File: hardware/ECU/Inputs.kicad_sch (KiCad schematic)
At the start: 39 parts, among them U12 LMV324LIDT, U13 SP720

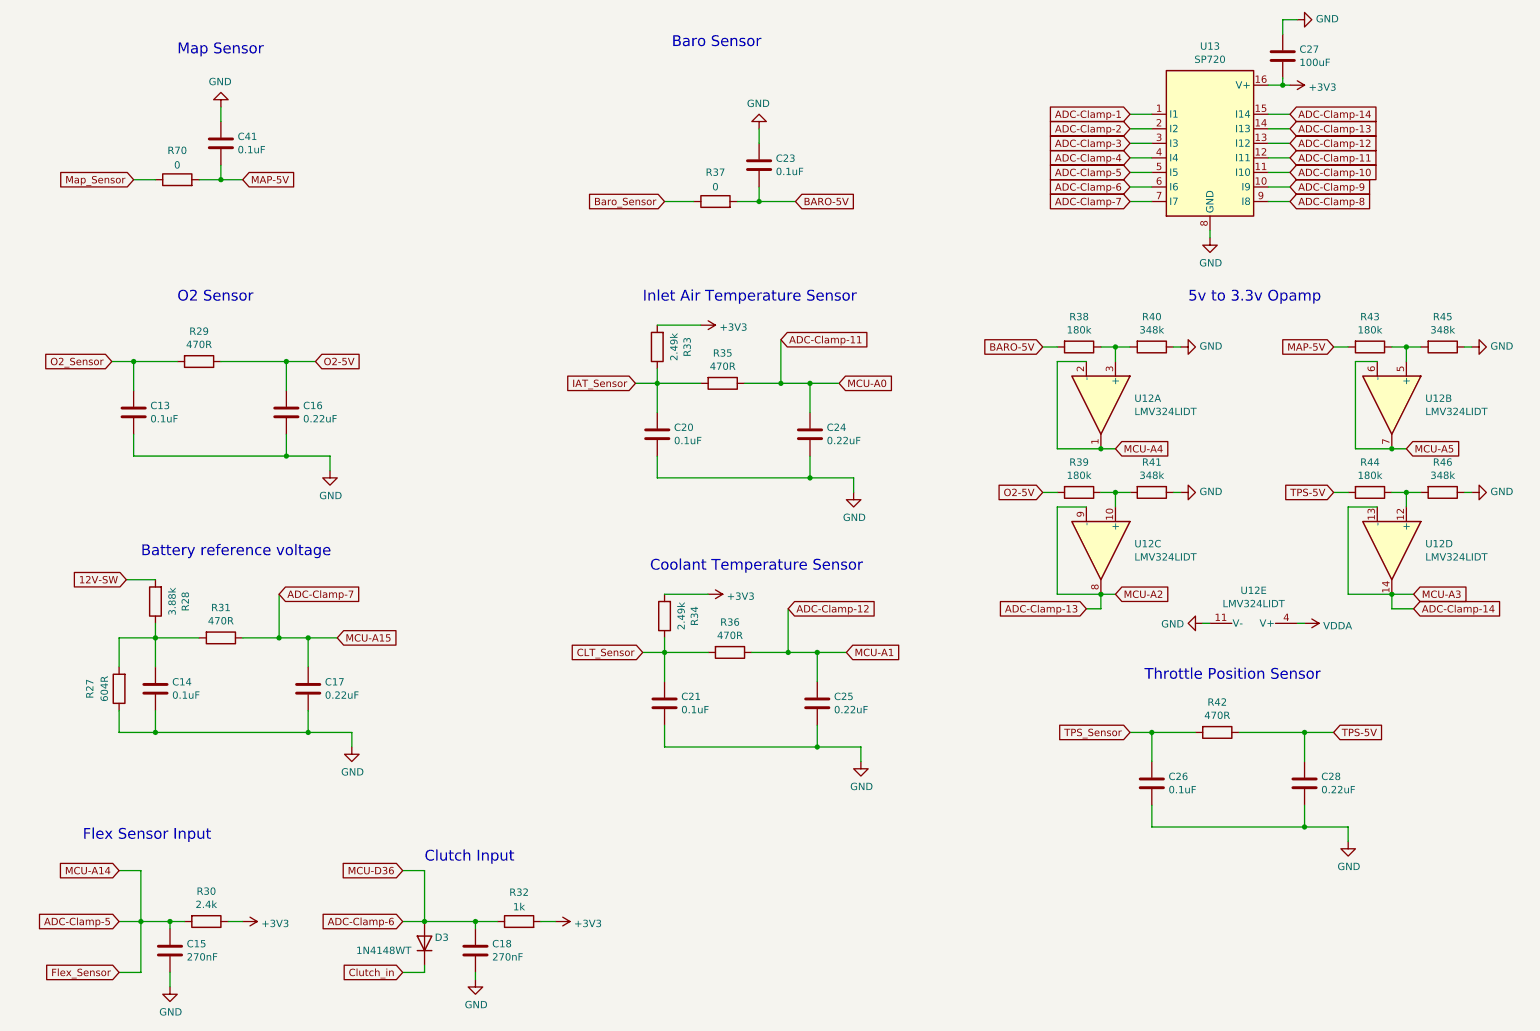
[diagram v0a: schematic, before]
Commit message: Replace speeduino submodule with HasiKe fork, fix teensy.pretty path
- Switch speeduino from speeduino/speeduino to HasiKe/speeduino
- Fix teensy.pretty submodule path case mismatch (Hardware -> hardware)
- Add ISL9V5036P3-F085 component library
- Various ECU schematic updates
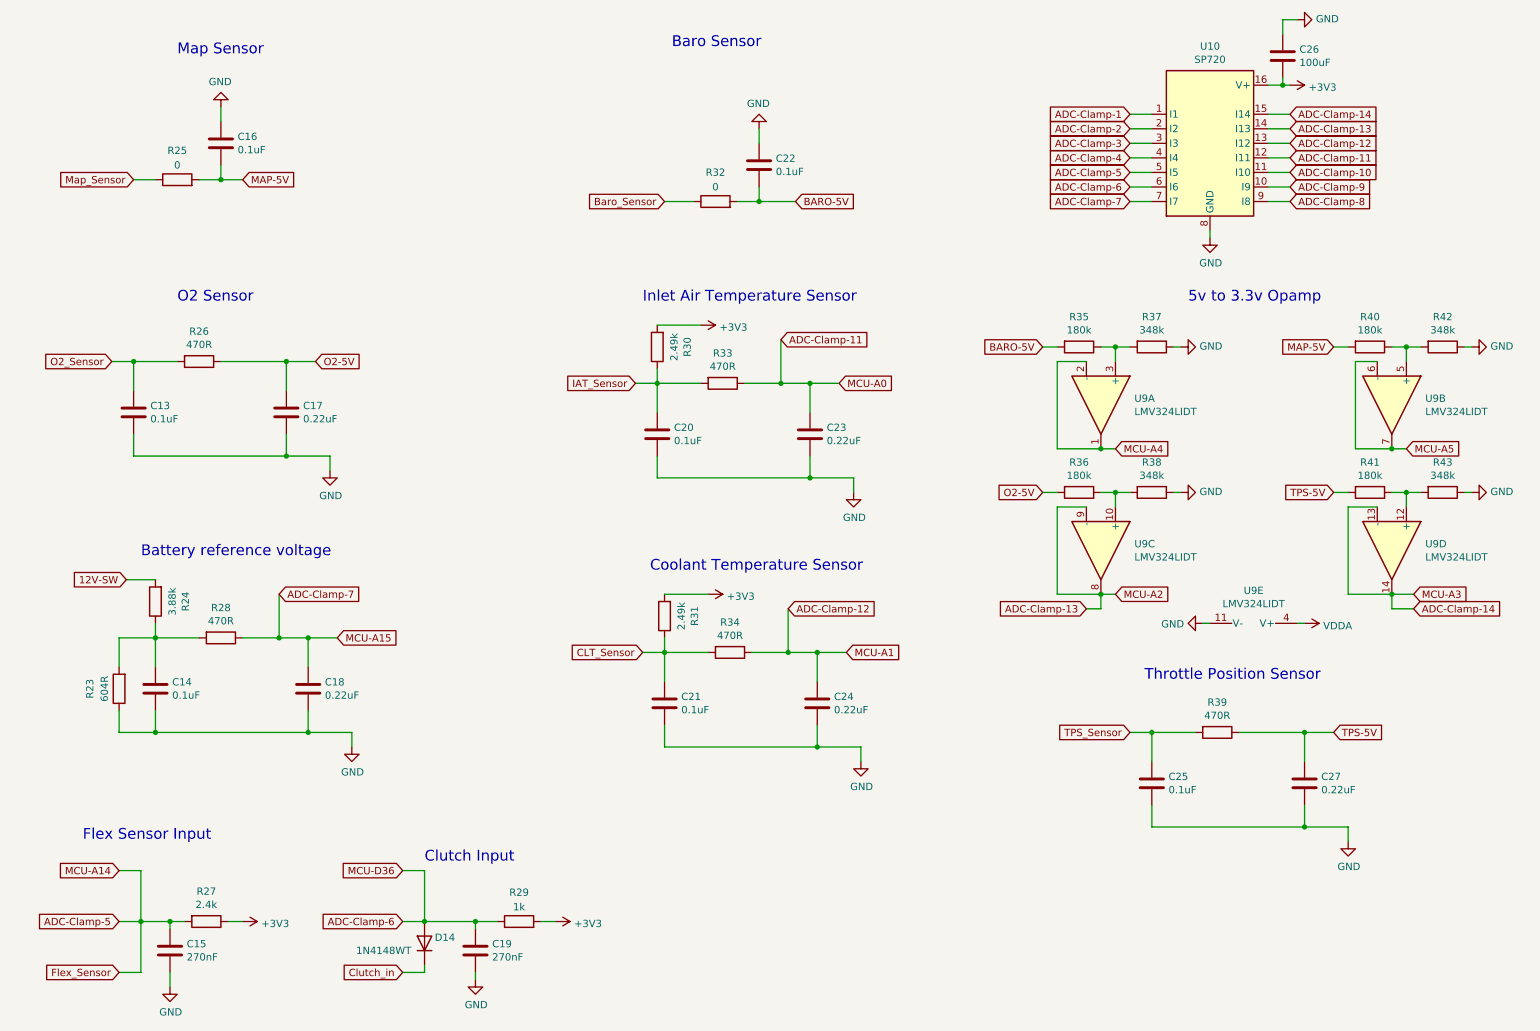
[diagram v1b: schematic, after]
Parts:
- renumbered C41 to C16, C16 to C17, C17 to C18, C18 to C19, C23 to C22, C24 to C23, C25 to C24, C26 to C25, C27 to C26, C28 to C27, D3 to D14, R27 to R23, R28 to R24, R70 to R25, R29 to R26, R30 to R27, R31 to R28, R32 to R29, R33 to R30, R34 to R31, R37 to R32, R35 to R33, R36 to R34, R38 to R35, R39 to R36, R40 to R37, R41 to R38, R42 to R39, R43 to R40, R44 to R41, R45 to R42, R46 to R43, U13 to U10, U12 to U9
